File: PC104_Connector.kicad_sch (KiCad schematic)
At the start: 2 parts

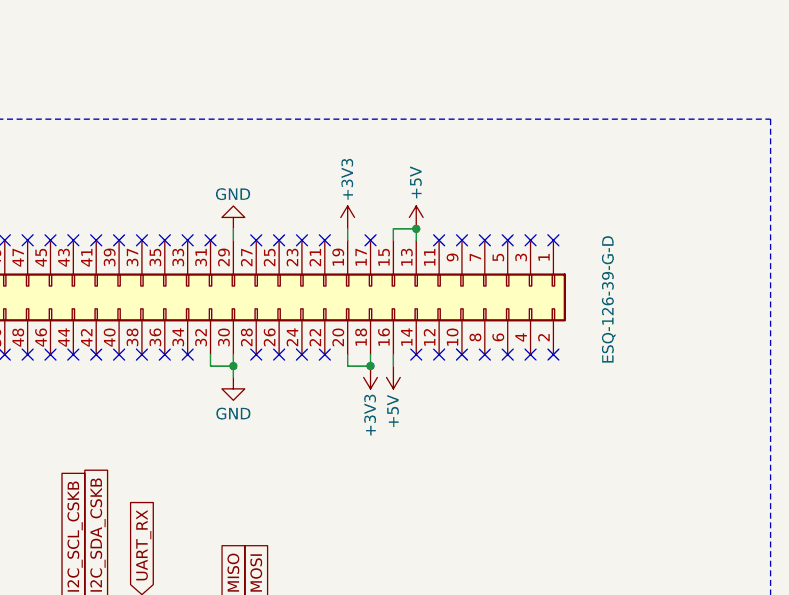
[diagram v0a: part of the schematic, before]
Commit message: Moved SD Card Slot
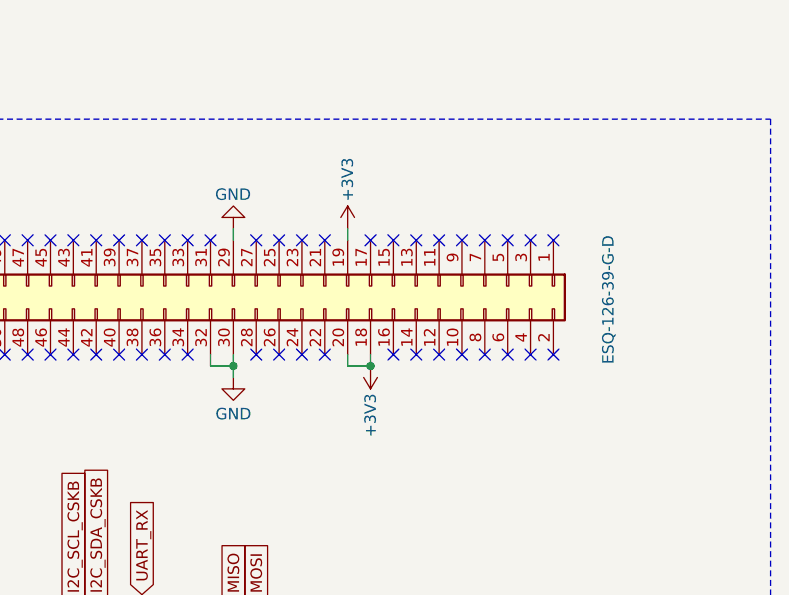
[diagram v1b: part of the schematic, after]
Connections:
- removed net +5V: H2.13 (Pin_13), H2.15 (Pin_15), H2.16 (Pin_16)
- no-connect marks 85 -> 88
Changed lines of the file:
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@@
-	)
-	(junction
-		(at 167.64 57.15)
-		(diameter 0)
-		(color 0 0 0 0)
 	)
 	(junction
@@
 	)
 	(no_connect
+		(at 167.64 58.42)
+	)
+	(no_connect
 		(at 154.94 113.03)
 	)
@@
 	)
 	(no_connect
+		(at 165.1 58.42)
+	)
+	(no_connect
 		(at 137.16 71.12)
 	)
@@
 	)
 	(no_connect
+		(at 165.1 71.12)
+	)
+	(no_connect
 		(at 175.26 113.03)
 	)
@@
 	(wire
 		(pts
-			(xy 165.1 71.12) (xy 165.1 72.39)
-		)
-		(stroke
-			(width 0)
-			(type default)
-		)
-	)
-	(wire
-		(pts
 			(xy 119.38 99.06) (xy 119.38 100.33)
 		)
@@
 	(wire
 		(pts
-			(xy 167.64 57.15) (xy 165.1 57.15)
-		)
-		(stroke
-			(width 0)
-			(type default)
-		)
-	)
-	(wire
-		(pts
 			(xy 147.32 99.06) (xy 147.32 100.33)
-		)
-		(stroke
-			(width 0)
-			(type default)
-		)
-	)
-	(wire
-		(pts
-			(xy 165.1 57.15) (xy 165.1 58.42)
-		)
-		(stroke
-			(width 0)
-			(type default)
-		)
-	)
-	(wire
-		(pts
-			(xy 167.64 57.15) (xy 167.64 58.42)
 		)
 		(stroke
@@
 	)
 	(symbol
-		(lib_id "power:+5V")
-		(at 165.1 72.39 180)
-		(unit 1)
-		(exclude_from_sim no)
-		(in_bom yes)
-		(on_board yes)
-		(dnp no)
-		(property "Reference" "#PWR02"
-			(at 165.1 68.58 0)
-			(effects
-				(font
-					(size 1.27 1.27)
-				)
-				(hide yes)
-			)
-		)
-		(property "Value" "+5V"
-			(at 165.1 77.47 90)
-			(effects
-				(font
-					(size 1.27 1.27)
-				)
-			)
-		)
-		(property "Footprint" ""
-			(at 165.1 72.39 0)
-			(effects
-				(font
-					(size 1.27 1.27)
-				)
-				(hide yes)
-			)
-		)
-		(property "Datasheet" ""
-			(at 165.1 72.39 0)
-			(effects
-				(font
-					(size 1.27 1.27)
-				)
-				(hide yes)
-			)
-		)
-		(property "Description" "Power symbol creates a global label with name \"+5V\""
-			(at 165.1 72.39 0)
-			(effects
-				(font
-					(size 1.27 1.27)
-				)
-				(hide yes)
-			)
-		)
-		(pin "1"
-		)
-		(instances
-			(project "adapter-pcb"
-				(path "/94da9b83-1146-4f01-8e34-8153765b0257/6da06bd5-7839-43dd-9065-41aec0431e8e"
-					(reference "#PWR02")
-					(unit 1)
-				)
-			)
-		)
-	)
-	(symbol
 		(lib_id "power:GND")
 		(at 147.32 57.15 180)
@@
 					(unit 1)
 				)
-			)
-		)
-	)
-	(symbol
-		(lib_id "power:+5V")
-		(at 167.64 57.15 0)
-		(unit 1)
-		(exclude_from_sim no)
-		(in_bom yes)
-		(on_board yes)
-		(dnp no)
-		(property "Reference" "#PWR01"
-			(at 167.64 60.96 0)
-			(effects
-				(font
-					(size 1.27 1.27)
-				)
-				(hide yes)
-			)
-		)
-		(property "Value" "+5V"
-			(at 167.64 52.07 90)
-			(effects
-				(font
-					(size 1.27 1.27)
-				)
-			)
-		)
-		(property "Footprint" ""
-			(at 167.64 57.15 0)
-			(effects
-				(font
-					(size 1.27 1.27)
-				)
-				(hide yes)
-			)
-		)
-		(property "Datasheet" ""
-			(at 167.64 57.15 0)
-			(effects
-				(font
-					(size 1.27 1.27)
-				)
-				(hide yes)
-			)
-		)
-		(property "Description" "Power symbol creates a global label with name \"+5V\""
-			(at 167.64 57.15 0)
-			(effects
-				(font
-					(size 1.27 1.27)
-				)
-				(hide yes)
-			)
-		)
-		(pin "1"
-		)
-		(instances
-			(project "adapter-pcb"
-				(path "/94da9b83-1146-4f01-8e34-8153765b0257/6da06bd5-7839-43dd-9065-41aec0431e8e"
-					(reference "#PWR01")
-					(unit 1)
-				)
